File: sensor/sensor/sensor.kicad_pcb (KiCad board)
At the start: 4 copper layers, 60 x 21 mm, 61 parts, among them J1 RJ12_Shielded, J2 Conn_01x04, J3 Conn_01x06, J4 Conn_01x03_Socket, J5 Conn_01x03_Socket, J6 Conn_01x03_Socket, J7 Conn_01x03_Socket, SW5 SW_Coded_SH-7050, U1 PCA9615DP, U2 LTC4316xDD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

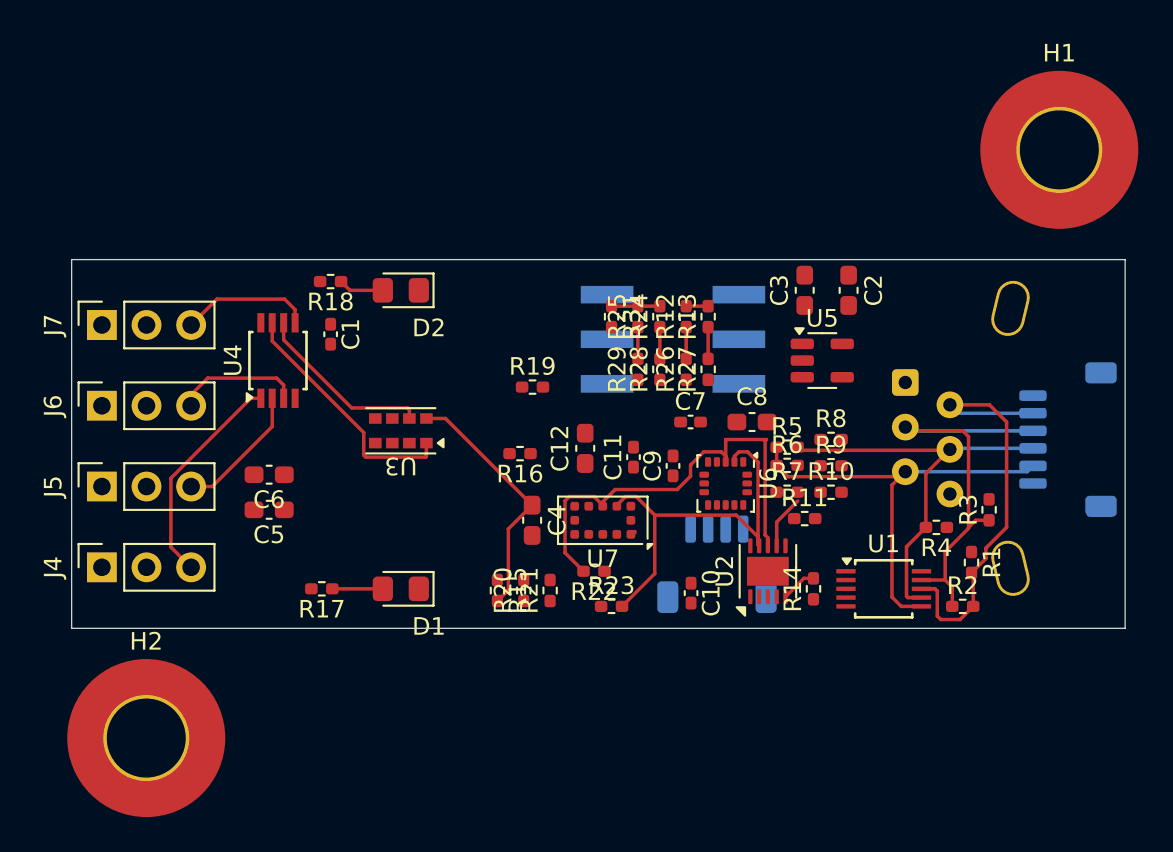
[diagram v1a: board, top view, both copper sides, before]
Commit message: finished traces but forgor output RJ12
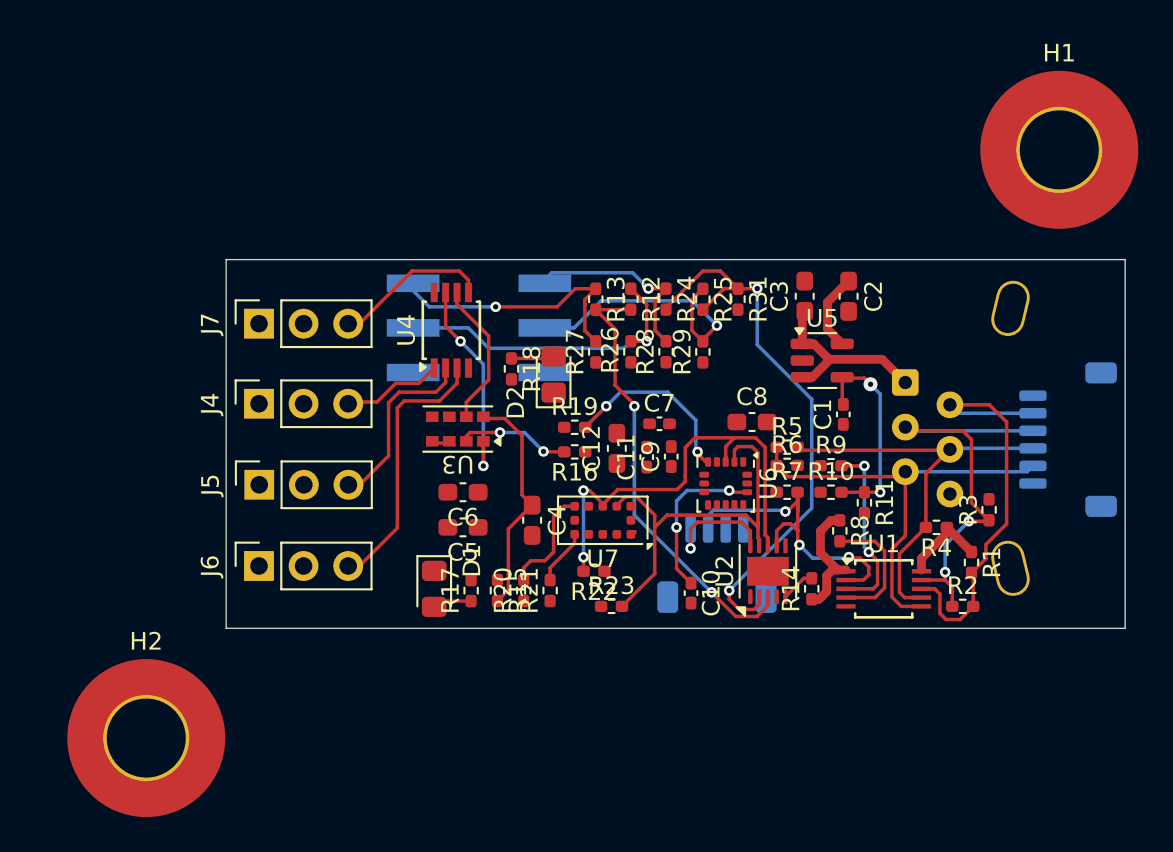
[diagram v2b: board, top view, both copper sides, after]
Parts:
- moved C1 29.6 mm to (93.2, 62.6), turned to 90 degrees
- moved J4 12.9 mm to (59.9, 62.0)
- moved J6 12.8 mm to (59.9, 71.2)
- moved R18 11.4 mm to (74.3, 60.0), turned to -90 degrees
- moved C5 11.1 mm to (71.5, 69.0)
- moved C6 11.1 mm to (71.5, 67.0)
- moved SW5 11.1 mm to (72.4, 62.6)
- moved U4 10.0 mm to (70.9, 57.8)
- moved D2 9.94 mm to (76.7, 60.3), turned to 90 degrees
- moved J5 8.96 mm to (59.9, 66.6)
- moved J7 8.95 mm to (59.9, 57.4)
- moved R17 8.50 mm to (72.0, 72.6), turned to 90 degrees
- moved R31 7.27 mm to (87.2, 56.0)
- moved R13 6.48 mm to (79.1, 56.0), turned to -90 degrees
- moved R27 6.48 mm to (79.1, 59.0)
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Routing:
- net Net-(U2-XORH): track 2.75 -> 32.5 mm, vias 0 -> 2
- net Net-(U2-XORL): track 1.25 -> 25.7 mm, vias 0 -> 2
- net Net-(R12-Pad1): track 1.81 -> 18.4 mm, vias 0 -> 1
- net Net-(J2-Pin_3): track 3.05 -> 19.2 mm, vias 0 -> 3
- net +5V: track 0.00 -> 15.7 mm
- net Net-(R25-Pad1): track 1.81 -> 16.0 mm, vias 0 -> 1
- net Net-(J2-Pin_4): track 0.00 -> 14.1 mm, vias 0 -> 1
- net Net-(R13-Pad1): track 1.81 -> 15.6 mm, vias 0 -> 1
- net Net-(U5-FB): track 0.00 -> 11.9 mm, vias 0 -> 2
- net +3.3V: track 0.00 -> 11.5 mm
- net Net-(U6-~{CS}): track 0.00 -> 10.5 mm, vias 0 -> 2
- net Net-(U1-EN): track 0.00 -> 10.3 mm, vias 0 -> 2
- net Net-(R24-Pad1): track 1.81 -> 11.2 mm, vias 0 -> 1
- net Net-(U6-REGOUT): track 0.00 -> 9.34 mm, vias 0 -> 2
- net Net-(J6-Pin_3): track 7.21 -> 15.4 mm
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- added copper zone on In1.Cu, net +3.3V
- added copper zone on In1.Cu, net +5V
- added copper zone on In2.Cu, net GND
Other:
- board size 60 x 21 mm -> 51.2 x 21 mm

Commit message: finished board pre adding output RJ12
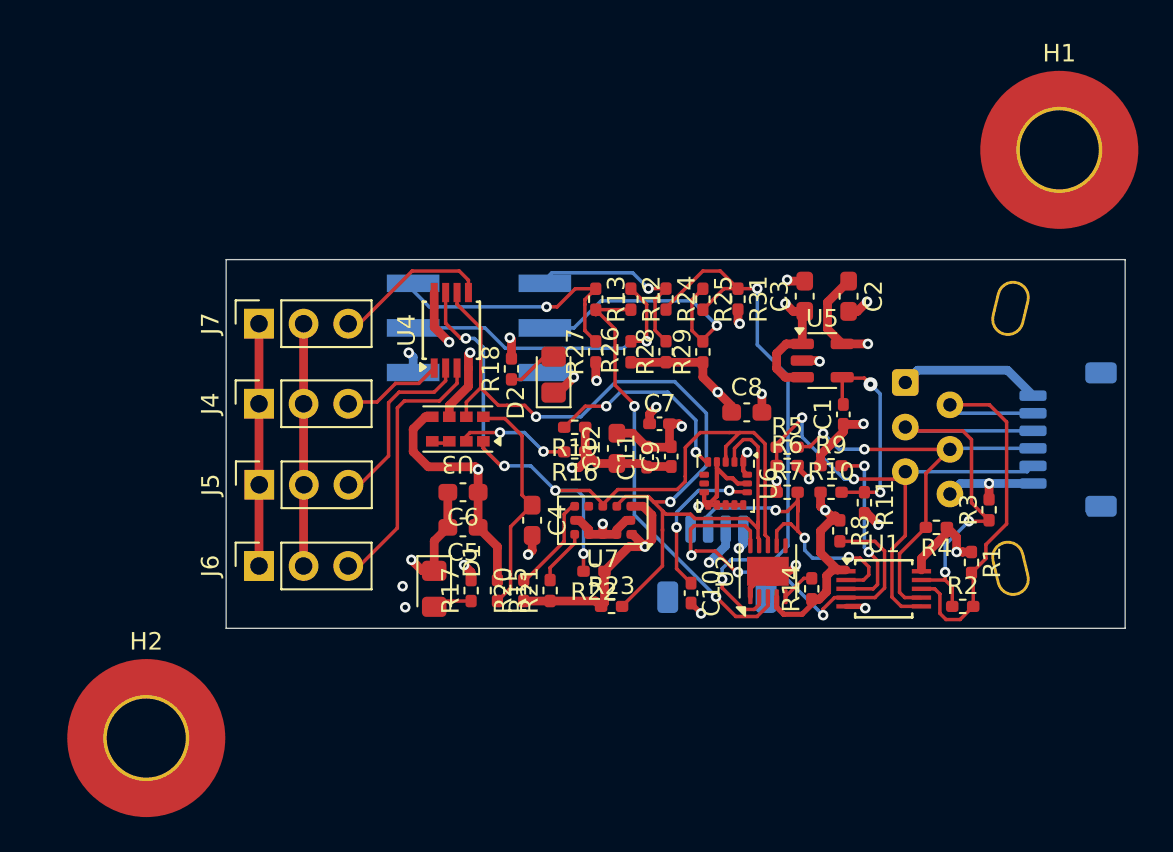
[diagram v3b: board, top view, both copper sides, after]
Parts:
- moved C8 0.63 mm to (87.7, 62.5)
- turned R18 to 90 degrees
- turned R19 to 180 degrees
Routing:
- net GND: track 1.17 -> 79.4 mm, vias 0 -> 21
- net +3.3V: track 11.5 -> 73.2 mm, vias 0 -> 12
- net +5V: track 15.7 -> 45.9 mm, vias 0 -> 6
- net /Sensors/scl: track 31.5 -> 54.4 mm, vias 0 -> 2
- net Net-(J2-Pin_4): track 14.1 -> 25.8 mm, vias 1 -> 3
- net /Sensors/sda: track 38.3 -> 47.3 mm
- net Net-(J3-Pin_5): track 25.5 -> 28.2 mm, vias 0 -> 2
- net Net-(U6-~{CS}): track 10.5 -> 11.8 mm
- net Net-(J3-Pin_4): track 24.2 -> 25.2 mm, vias 0 -> 2
- net Net-(U7-GPIO1): track 6.22 -> 5.55 mm
- net Net-(D2-A): track 2.44 -> 3.11 mm
- net Net-(U2-XORH): track 32.5 -> 33.0 mm
